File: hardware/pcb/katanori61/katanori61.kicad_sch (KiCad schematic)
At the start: 55 parts, among them J1 XIAO RISER, J10 BAT (JST-PH), J13 USB-C, J2 OLED, J4 SPK IN, J5 SPK OUT, J6 BTN2, J7 REED+TOGGLE, K31 G6S-2F DC5, Q1 MMUN2133LT1G, Q2 AO3401A, Q31 SS8050, U1 TPS61090RSAR, U2 MCP73871-2CCI/ML, U3 INA226AIDGSR, U4 AS5600-ASOM

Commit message: pcb v6.1: AS5600 を ASOT C499458 へ（ASOM C79815 とはリールの大きさだけ違う・📄 データシート 38 ページ。在庫 378 → 6726・単価 $1.76 → $1.36。JLCPCB のプレビューで U4 の向きを確かめた）
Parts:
- U4: value AS5600-ASOM -> AS5600-ASOT; LCSC C79815 -> C499458
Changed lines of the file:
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@@
 			)
 		)
-		(property "Value" "AS5600-ASOM"
+		(property "Value" "AS5600-ASOT"
 			(at 347.98 173.38 0)
 			(effects
@@
 			)
 		)
-		(property "LCSC" "C79815"
+		(property "LCSC" "C499458"
 			(at 347.98 165.10 0)
 			(effects

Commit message: pcb v6.1: MCP73871 をテープ＆リール品 C511310（MCP73871T-2CCI/ML）へ（T は梱包だけ・📄 データシート PRODUCT IDENTIFICATION。$4.41 → $2.19・在庫 2410。5 枚の見積り $110.68 → $99.52。JLCPCB のプレビューで U2 の向きを確かめた）
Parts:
- U2: LCSC C5121473 -> C511310
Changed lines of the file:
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@@
 			)
 		)
-		(property "LCSC" "C5121473"
+		(property "LCSC" "C511310"
 			(at 43.18 154.94 0)
 			(effects

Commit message: pcb v6.1: 表示灯を外す（LED1〜4・R5・R8・R14・R20・Q1 の 9 個）／C7 を U2 の VLIPO の隣へ
- ユーザー「LED は本来不要」。PowerBoost の LED 4 つとそれだけに要る 5 個を回路図と板から消した。
  LBO・STAT1・STAT2 はオープンドレインなので何もつながない。LBI の分圧 R1・R2 は残す
  （📄 TPS61090 9.3.7「LBI を浮かせない」）。check_sch.py の DROPPED に同じ 9 個
- 引き直しで C7（VLIPO）への枝が内層 11.4mm・21mΩ になった（前も裏 7.5mm）。C6・C9 と同じ轍なので
  C7 を U2 の 16 番の右上へ寄せ、c7_link・u2_16_link で先に引く（VLIPO 16.2 → 3.3mm・17 → 5mΩ）。
  C41 は U3 の V33 の真上へ（3.6 → 2.1mm）、R6・R7 は空いた列へ
- DRC エラー 0・未接続 0・すきま不足 0・シルクを絵で確認・筐体の当たり 新しい 0 件（レジン・ナイロン）・
  check_fab 合わない所なし。部品 30 種類 48 個 → 25 種類 39 個（拡張 9 種類）
- ⚠ pad_box() は 90°／270° の部品で幅と高さを入れ替えて返す（c7_link は避けて書いた。関数は未修正）
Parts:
- removed C31: 0.1uF, Capacitor_SMD:C_0805_2012Metric, symbol Device:C_Small
- removed LED1: RED, LED_SMD:LED_0805_2012Metric, symbol Device:LED_Small
- removed LED2: WHITE, LED_SMD:LED_0805_2012Metric, symbol Device:LED_Small
- removed LED3: GREEN, LED_SMD:LED_0805_2012Metric, symbol Device:LED_Small
- removed LED4: YELLOW, LED_SMD:LED_0805_2012Metric, symbol Device:LED_Small
- removed Q1: MMUN2133LT1G, Package_TO_SOT_SMD:SOT-23, symbol Transistor_BJT:Q_PNP_BRT_BEC
- removed R14, R20, R5, R8: 1K, Resistor_SMD:R_0805_2012Metric, symbol Device:R_Small
- removed R44, R45: 5.1k, Resistor_SMD:R_0805_2012Metric, symbol Device:R_Small
- added C41: 0.1uF, Capacitor_SMD:C_0805_2012Metric, symbol Device:C_Small
- added R41: 10m, Resistor_SMD:R_1206_3216Metric, symbol Device:R_Small
- added R42: 10K, Resistor_SMD:R_0805_2012Metric, symbol Device:R_Small
- C31: renamed from Q2; value AO3401A -> 0.1uF; footprint Package_TO_SOT_SMD:SOT-23 -> Capacitor_SMD:C_0805_2012Metric; symbol Transistor_FET:Q_PMOS_GSD -> Device:C_Small; LCSC C15127 -> C49678; Note 逆接保護（P-ch）。1=G・2=S・3=D は AO3401A の SOT-23 の並び。📄 LCSC C15127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 -> relay_board C1
- Q2: renamed from R42; value 10K -> AO3401A; footprint Resistor_SMD:R_0805_2012Metric -> Package_TO_SOT_SMD:SOT-23; symbol Device:R_Small -> Transistor_FET:Q_PMOS_GSD; LCSC C17414 -> C15127; Note I2C の引き上げ -> 逆接保護（P-ch）。1=G・2=S・3=D は AO3401A の SOT-23 の並び。📄 LCSC C15127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
- R44: renamed from R41; value 10m -> 5.1k; footprint Resistor_SMD:R_1206_3216Metric -> Resistor_SMD:R_0805_2012Metric; LCSC C105362 -> C27834; Note シャント 10mΩ（今のモジュールと同じ値）。🔴 ケルビン必須 — gen_pcb.py の PRE_TRACKS を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 -> CC1 の引き下げ（充電器に 5V を出させる）
- R45: renamed from C41; value 0.1uF -> 5.1k; footprint Capacitor_SMD:C_0805_2012Metric -> Resistor_SMD:R_0805_2012Metric; symbol Device:C_Small -> Device:R_Small; LCSC C49678 -> C27834; Note (none) -> CC2 の引き下げ
- U2: Note 充電・ロードシェア（PowerBoost U2） -> 充電・ロードシェア（PowerBoost U2）。MCP73871T-2CCI/ML ── T はテープ＆リールだけ（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
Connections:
- net BATG: now also Q2.1 (G); no longer C31.1 (G)
- net BATP: now also Q2.2 (S), R41.1; no longer C31.2 (S), R44.1
- net BATRAW: now also Q2.3 (D); no longer C31.3 (D)
- net CC1: now also R44.1
- net CC2: now also R45.1
- net GND: now also C31.2, R44.2, C41.2
- net SDA: now also R42.2; no longer Q2.2
- net V33: now also C41.1, R42.1; no longer Q2.1, R45.1
- net V5: now also C31.1
- net VLIPO: now also R41.2; no longer R44.2
- net LBO: no longer names the net of U1.12 (LBO)
- net STAT1: no longer names the net of U2.8 (STAT1/~{LBO})
- net STAT2: no longer names the net of U2.7 (STAT2)
- no-connect marks 15 -> 18
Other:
- moved on the sheet: R44

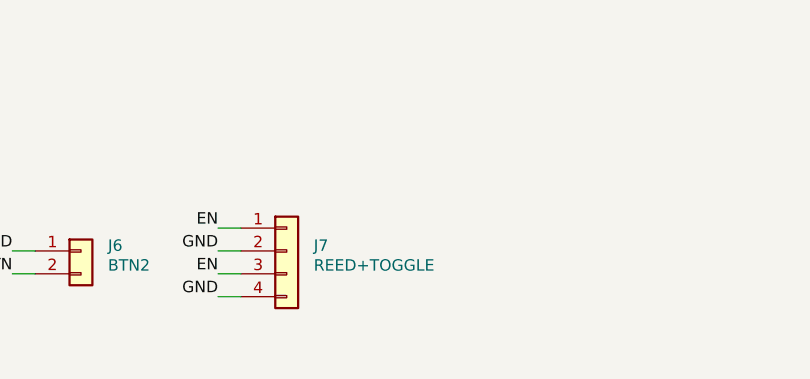
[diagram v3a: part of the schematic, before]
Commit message: v6.1: 電源をハッチのトグルから PCB の押しボタン SW2（XKB5858-Z-E）へ／つまみを左へ 2.0・軸ガイドの穴 3 つ／つまみの台座を直す
電源（🔒 ユーザー 2026-09-19）
- ハッチのトグル MTS-102（座・M6 の穴・線 2 本）をやめ、PCB の後ろの縁、USB-C の左隣に横向き・自己保持の押しボタン SW2（XKB5858-Z-E・LCSC C780038・押し子 5.0）
- 接点 1 GND・3 EN（1–3 は出ている間に閉 ＝ OFF。接点の図とピンの前後の並びの両方から確定）。J7 はリードだけの 2 ピン
- 押し子に丸いキャップ（φ6.6・顔の芯を USB-C の口の芯の高さに揃える・鍔で抜け止め・顔に電源の記号）。キャップは光造形で刷る（print_pwrcap）。断面の模型 part="look_pwrcap"
- 後ろの壁に φ7.1 の丸穴。PCB を入れるときの前逃がし pcb_fwd 1.8 → 3.6（キャップの顔）。C31 は SW2 と重なったので SW2 の前へ固定
- 足形 katanori.pretty/SW_XKB5858-Z-E（パッドは JLC の足形のまま）と記号を追加。parts/mts102_v61.scad を削除

つまみ
- 軸を左へ 2.0（v61_board.SHAFT・KNOB_AT 67.7 → 65.7）。U4・C42・立入禁止・電池の線の道は SHAFT から引く
- 軸ガイドの足の穴 3 つ（M2 φ2.2・半径 12・120° 等分）を取付穴の一覧へ
- 天板の台座: 足 4 本を高さで切り落として段（ナットの六角穴と E リングの受け）ごと消していたのを戻す（knob_station_add(arms=false)）
- リードの穴の入口を掘り上げて押し込む距離 8.0 → 4.5（天井は据え置き）。右後ろの隅を柱の逃げの外まで丸める
- E リングを 1 枚ずつ色分けし、分解図で上下に離す

検査: 回路図 0 件・DRC 未接続 0・製造ファイル「合わない所なし」。当たり・入れる道はナイロン／レジンとも新しい当たり 0（トグルの線と E リングの当たりは線ごと消えた）
格子・支柱・部品表・3D 模型・製造ファイル・発注用 STL を作り直した。組み立てマニュアルは文と番号だけ直した（挿絵と HTML は未）
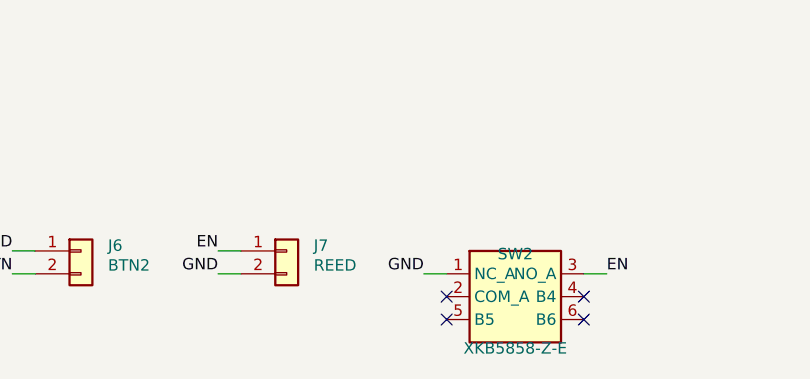
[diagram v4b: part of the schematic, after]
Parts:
- added SW2: XKB5858-Z-E, katanori:SW_XKB5858-Z-E, symbol katanori:SW_XKB5858-Z-E
- J7: value REED+TOGGLE -> REED; footprint Connector_JST:JST_PH_B4B-PH-K_1x04_P2.00mm_Vertical -> Connector_JST:JST_PH_B2B-PH-K_1x02_P2.00mm_Vertical; symbol Connector_Generic:Conn_01x04 -> Connector_Generic:Conn_01x02; Note 1 EN・2 GND → リード ／ 3 EN・4 GND → マスタートグル（縦の口・上から挿す） -> 1 EN・2 GND → リード（縦の口・上から挿す）
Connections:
- net EN: now also SW2.3 (NO_A); no longer J7.3 (Pin_3)
- net GND: now also SW2.1 (NC_A); no longer J7.4 (Pin_4)
- no-connect marks 18 -> 22
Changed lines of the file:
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@@
 	)
 	(symbol
-		(lib_id "Connector_Generic:Conn_01x04")
+		(lib_id "Connector_Generic:Conn_01x02")
 		(at 132.08 243.84 0)
 		(unit 1)
@@
 			)
 		)
-		(property "Value" "REED+TOGGLE"
+		(property "Value" "REED"
 			(at 135.08 245.44 0)
 			(effects
@@
 			)
 		)
-		(property "Footprint" "Connector_JST:JST_PH_B4B-PH-K_1x04_P2.00mm_Vertical"
+		(property "Footprint" "Connector_JST:JST_PH_B2B-PH-K_1x02_P2.00mm_Vertical"
 			(at 132.08 243.84 0)
 			(effects
@@
 			)
 		)
-		(property "Note" "1 EN・2 GND → リード ／ 3 EN・4 GND → マスタートグル（縦の口・上から挿す）"
+		(property "Note" "1 EN・2 GND → リード（縦の口・上から挿す）"
 			(at 132.08 243.84 0)
 			(effects
@@
 		)
 		(pin "2"
-		)
-		(pin "3"
-		)
-		(pin "4"
 		)
 		(instances
@@
 	(wire
 		(pts
-			(xy 127.00 241.30)
-			(xy 124.46 241.30)
-		)
-		(stroke
-			(width 0)
-			(type default)
-		)
-	)
-	(label "EN"
-		(at 124.46 241.30 180)
-		(effects
-			(font
-				(size 1.27 1.27)
-			)
-			(justify right bottom)
-		)
-	)
-	(wire
-		(pts
 			(xy 127.00 243.84)
 			(xy 124.46 243.84)
@@
 		)
 	)
-	(label "GND"
+	(label "EN"
 		(at 124.46 243.84 180)
 		(effects
@@
 		)
 	)
+	(label "GND"
+		(at 124.46 246.38 180)
+		(effects
+			(font
+				(size 1.27 1.27)
+			)
+			(justify right bottom)
+		)
+	)
+	(symbol
+		(lib_id "katanori:SW_XKB5858-Z-E")
+		(at 157.48 248.92 0)
+		(unit 1)
+		(exclude_from_sim no)
+		(in_bom yes)
+		(on_board yes)
+		(dnp no)
+		(property "Reference" "SW2"
+			(at 157.48 244.18 0)
+			(effects
+				(font
+					(size 1.27 1.27)
+				)
+			)
+		)
+		(property "Value" "XKB5858-Z-E"
+			(at 157.48 254.66 0)
+			(effects
+				(font
+					(size 1.27 1.27)
+				)
+			)
+		)
+		(property "Footprint" "katanori:SW_XKB5858-Z-E"
+			(at 157.48 248.92 0)
+			(effects
+				(font
+					(size 1.27 1.27)
+				)
+				(hide yes)
+			)
+		)
+		(property "Datasheet" ""
+			(at 157.48 248.92 0)
+			(effects
+				(font
+					(size 1.27 1.27)
+				)
+				(hide yes)
+			)
+		)
+		(property "LCSC" "C780038"
+			(at 157.48 248.92 0)
+			(effects
+				(font
+					(size 1.27 1.27)
+				)
+				(hide yes)
+			)
+		)
+		(property "Note" "電源の押しボタン（板の後ろの縁・押し子は後ろの壁から出る）。1 GND・3 EN"
+			(at 157.48 248.92 0)
+			(effects
+				(font
+					(size 1.27 1.27)
+				)
+				(hide yes)
+			)
+		)
+		(pin "1"
+		)
+		(pin "2"
+		)
+		(pin "5"
+		)
+		(pin "3"
+		)
+		(pin "4"
+		)
+		(pin "6"
+		)
+		(instances
+			(project "katanori61"
+				(path "/377120ba-3fb3-530c-9f35-c36cf0274025"
+					(reference "SW2")
+					(unit 1)
+				)
+			)
+		)
+	)
+	(wire
+		(pts
+			(xy 149.86 246.38)
+			(xy 147.32 246.38)
+		)
+		(stroke
+			(width 0)
+			(type default)
+		)
+	)
+	(label "GND"
+		(at 147.32 246.38 180)
+		(effects
+			(font
+				(size 1.27 1.27)
+			)
+			(justify right bottom)
+		)
+	)
+	(no_connect
+		(at 149.86 248.92)
+	)
+	(no_connect
+		(at 149.86 251.46)
+	)
+	(wire
+		(pts
+			(xy 165.10 246.38)
+			(xy 167.64 246.38)
+		)
+		(stroke
+			(width 0)
+			(type default)
+		)
+	)
 	(label "EN"
-		(at 124.46 246.38 180)
-		(effects
-			(font
-				(size 1.27 1.27)
-			)
-			(justify right bottom)
-		)
-	)
-	(wire
-		(pts
-			(xy 127.00 248.92)
-			(xy 124.46 248.92)
-		)
-		(stroke
-			(width 0)
-			(type default)
-		)
-	)
-	(label "GND"
-		(at 124.46 248.92 180)
-		(effects
-			(font
-				(size 1.27 1.27)
-			)
-			(justify right bottom)
-		)
+		(at 167.64 246.38 0)
+		(effects
+			(font
+				(size 1.27 1.27)
+			)
+			(justify left bottom)
+		)
+	)
+	(no_connect
+		(at 165.10 248.92)
+	)
+	(no_connect
+		(at 165.10 251.46)
 	)
 	(symbol

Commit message: pcb v6.1: 低電池の分圧を外して LBI を GND へ／詰まっていた 4 組を開ける／角度センサの座標を式に
・R1 1.87M・R2 330K（低電池の分圧）を外し、LBI（U1 の 9 番）を GND へ直結。
  LBO は未接続で閾値 3.33V を誰も読まず、低電池は INA226 が I2C で読むので重複していた。
  📄 TPS61090/91/92 SLVS484C 12 ページ 9.3.7「使わないなら LBI は GND（か VBAT）へ繋げ。
  LBO は繋がなくてよい」── 浮かせなければよいのではなく繋げと書いてあり、分圧である必要は無い。
  機械に載せる部品 39 → 37 個・JLCPCB へ出す品番 26 → 24 種類（330kΩ C23137 は R2 だけが使っていた）。
  ⚠ 2026-09-19 に「分圧は残した」と POWER.md に書かれていたが、それは 🔒 の段落の中に
  AI 側がその場で決めた物を混ぜて書いたもので、ユーザーには聞いていなかった。

・胴どうしが 1mm を切っていた 4 組を開けた。R31–R32 0.75 → 1.55・R44–R45 0.85 → 1.60・
  R42–R43 0.85 → 1.45・R46–J2 0.94 → 1.44mm。R45 は VBUS の幹があるので動かさず、R44 だけ右へ。
  周りで狭くなった所は無い（いちばん近いのは Q2–R31 の 1.02mm で、前の 9 番目 0.98mm より広い）。
  板全体の最小は L1–R3 の 0.67mm のままにした。ここを開けるのは電源の塊をほどく話になる。

・v61_board.py の AS5600 = (65.7, 13.8) を消し、SHAFT から出す式にした。2026-09-19 に
  つまみを左へ 2.0 動かしたときの取り残しで、部品を置くコードは読んでいないので板は正しかったが、
  リレーとの距離の根拠だけ 2mm ずれていた。実測は 18.5mm・磁石の影響は 7.4 分の 1（20mm・9 分の 1 は誤り）。

・裏のシルクの日付を 2026-09-20 へ。

見送り: 音の 3 本（SPKM・SPKO・SPKP）を内層から外層へ手で引き直す案。284 → 150mΩ になるが、
8Ω に対して P ∝ R/(R+r)² なので 0.14dB にしかならず聞こえない。元の 720mΩ でさえ 0.35dB だった。
銅は測り直して 284mΩ（POWER.md の 208mΩ は 9/17 にリレーを角度センサの横から退ける前の値で、
退けたぶん SPKO が 25 → 49mm に伸びていた）。割合ではなく dB で見ること、を POWER.md に残した。

検査: 回路図の突き合わせ 0 件（写し元との意図した差に LBI を登録）・DRC 9 件（前と同じ取付穴の
足形 7・USB-C のシルクが縁で切れる 2）・未配線 0・回路図との食い違い 0・銅のすきま 0 件（最小 0.152）・
製造ファイルの照合 合わない所なし・掃引はナイロンとレジンとも「入る」新しい当たり 0 件。
電源の道は測り直して悪化なし（3.3V は自動配線が裏を使ったぶん 366 → 148mΩ）。
模型（v61_parts.scad・v61_parts3d.stl・v61_silk.scad）も作り直した。板と口の STL は中身が同じ。
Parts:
- removed J10: BAT (JST-PH), Connector_JST:JST_PH_B2B-PH-K_1x02_P2.00mm_Vertical, symbol Connector_Generic:Conn_01x02
- removed J13: USB-C, Connector_USB:USB_C_Receptacle_HRO_TYPE-C-31-M-12, symbol Connector:USB_C_Receptacle_USB2.0_16P
- removed J2: OLED, Connector_PinHeader_2.54mm:PinHeader_1x04_P2.54mm_Vertical, symbol Connector_Generic:Conn_01x04
- removed J5: SPK OUT, Connector_JST:JST_PH_S2B-PH-K_1x02_P2.00mm_Horizontal, symbol Connector_Generic:Conn_01x02
- removed Q2: AO3401A, Package_TO_SOT_SMD:SOT-23, symbol Transistor_FET:Q_PMOS_GSD
- removed Q31: SS8050, Package_TO_SOT_SMD:SOT-23, symbol Transistor_BJT:MMBT3904
- removed R15: 15K, Resistor_SMD:R_0805_2012Metric, symbol Device:R_Small
- removed R32: 10k, Resistor_SMD:R_0805_2012Metric, symbol Device:R_Small
- removed SW2: XKB5858-Z-E, katanori:SW_XKB5858-Z-E, symbol katanori:SW_XKB5858-Z-E
- removed U3: INA226AIDGSR, Package_SO:TSSOP-10_3x3mm_P0.5mm, symbol Sensor_Energy:INA226
- removed U4: AS5600-ASOT, Package_SO:SOIC-8_3.9x4.9mm_P1.27mm, symbol katanori:AS5600-ASOM
- added C31, C41, C42: 0.1uF, Capacitor_SMD:C_0805_2012Metric, symbol Device:C_Small
- added J4: SPK IN, Connector_JST:JST_PH_B2B-PH-K_1x02_P2.00mm_Vertical, symbol Connector_Generic:Conn_01x02
- added J6: BTN2, Connector_JST:JST_PH_B2B-PH-K_1x02_P2.00mm_Vertical, symbol Connector_Generic:Conn_01x02
- added R31: 1k, Resistor_SMD:R_0805_2012Metric, symbol Device:R_Small
- added R41: 10m, Resistor_SMD:R_1206_3216Metric, symbol Device:R_Small
- added R44: 5.1k, Resistor_SMD:R_0805_2012Metric, symbol Device:R_Small
- added R46: 100K, Resistor_SMD:R_0805_2012Metric, symbol Device:R_Small
- C7: renamed from R13; value 200K -> 10uF; footprint Resistor_SMD:R_0805_2012Metric -> Capacitor_SMD:C_0805_2012Metric; symbol Device:R_Small -> Device:C_Small; LCSC C17539 -> C15850
- C8: renamed from R2; value 330K -> 10uF; footprint Resistor_SMD:R_0603_1608Metric -> Capacitor_SMD:C_0805_2012Metric; symbol Device:R_Small -> Device:C_Small; LCSC C23137 -> C15850; Note PowerBoost は 340kΩ（E96・Extended）。LBO の閾値 0.5×(1+R1/R2) が 3.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 -> (none)
- J10: renamed from R42; value 10K -> BAT (JST-PH); footprint Resistor_SMD:R_0805_2012Metric -> Connector_JST:JST_PH_B2B-PH-K_1x02_P2.00mm_Vertical; symbol Device:R_Small -> Connector_Generic:Conn_01x02; LCSC C17414 -> (none); Note I2C の引き上げ -> 🔴 1 番が −・2 番が ＋（PowerBoost B1 の並び。⭐ 2026-09-16 夕から 2 番のネットは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
- J13: renamed from R43; value 10K -> USB-C; footprint Resistor_SMD:R_0805_2012Metric -> Connector_USB:USB_C_Receptacle_HRO_TYPE-C-31-M-12; symbol Device:R_Small -> Connector:USB_C_Receptacle_USB2.0_16P; LCSC C17414 -> C165948; Note I2C の引き上げ -> 充電の口。D+/D− と SBU は使わない。v6.1 は板の後ろの縁から 1.3 出し（⭐ 2026-09-17）で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
- J2: renamed from J4; value SPK IN -> OLED; footprint Connector_JST:JST_PH_B2B-PH-K_1x02_P2.00mm_Vertical -> Connector_PinHeader_2.54mm:PinHeader_1x04_P2.54mm_Vertical; symbol Connector_Generic:Conn_01x02 -> Connector_Generic:Conn_01x04; Note IN（ReSpeakerから） -> AS5600 へ4本（GNDは二股ケーブルでDIRへ）
- J5: renamed from C42; value 0.1uF -> SPK OUT; footprint Capacitor_SMD:C_0805_2012Metric -> Connector_JST:JST_PH_S2B-PH-K_1x02_P2.00mm_Horizontal; symbol Device:C_Small -> Connector_Generic:Conn_01x02; LCSC C49678 -> (none); Note AS5600 のパスコン（📄 9 ページ Figure 13） -> OUT（スピーカーへ）
- Q2: renamed from R44; value 5.1k -> AO3401A; footprint Resistor_SMD:R_0805_2012Metric -> Package_TO_SOT_SMD:SOT-23; symbol Device:R_Small -> Transistor_FET:Q_PMOS_GSD; LCSC C27834 -> C15127; Note CC1 の引き下げ（充電器に 5V を出させる） -> 逆接保護（P-ch）。1=G・2=S・3=D は AO3401A の SOT-23 の並び。📄 LCSC C15127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
- Q31: renamed from R31; value 1k -> SS8050; footprint Resistor_SMD:R_0805_2012Metric -> Package_TO_SOT_SMD:SOT-23; symbol Device:R_Small -> Transistor_BJT:MMBT3904; LCSC C17513 -> C2150; Note relay_board R1 -> relay_board Q1（2SC1815-GR の表面実装の代わり・SOT-23 は 1=B・2=E・3=C）
- R13: renamed from R1; value 1.87M -> 200K; LCSC C482988 -> C17539
- R15: renamed from R16; value 1.0K -> 15K; LCSC C17513 -> C17475; Note (none) -> PowerBoost THERM
- R16: renamed from R6; value 220K -> 1.0K; footprint Resistor_SMD:R_0603_1608Metric -> Resistor_SMD:R_0805_2012Metric; LCSC C22961 -> C17513; Note PowerBoost は 270kΩ（E96・Extended）。R7 と組で比を保つ -> (none)
- R17: renamed from R7; value 82K -> 100K; footprint Resistor_SMD:R_0603_1608Metric -> Resistor_SMD:R_0805_2012Metric; LCSC C23254 -> C149504; Note PowerBoost は 100kΩ。R6 と組で 100/370=0.2703 → 82/302=0.2715（差 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 -> (none)
- R32: renamed from R46; value 100K -> 10k; LCSC C149504 -> C17414; Note Q2 のゲートを GND へ落とす。電池は 3.0〜4.2V なので Vgs は最大 −4.2V で、AO3401A 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 -> relay_board R2・🔴 安全の要
- R42: renamed from R41; value 10m -> 10K; footprint Resistor_SMD:R_1206_3216Metric -> Resistor_SMD:R_0805_2012Metric; LCSC C105362 -> C17414; Note シャント 10mΩ（今のモジュールと同じ値）。🔴 ケルビン必須 — gen_pcb.py の PRE_TRACKS を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 -> I2C の引き上げ
- R43: renamed from C41; value 0.1uF -> 10K; footprint Capacitor_SMD:C_0805_2012Metric -> Resistor_SMD:R_0805_2012Metric; symbol Device:C_Small -> Device:R_Small; LCSC C49678 -> C17414; Note (none) -> I2C の引き上げ
- R6: renamed from C8; value 10uF -> 220K; footprint Capacitor_SMD:C_0805_2012Metric -> Resistor_SMD:R_0603_1608Metric; symbol Device:C_Small -> Device:R_Small; LCSC C15850 -> C22961; Note (none) -> PowerBoost は 270kΩ（E96・Extended）。R7 と組で比を保つ
- R7: renamed from C7; value 10uF -> 82K; footprint Capacitor_SMD:C_0805_2012Metric -> Resistor_SMD:R_0603_1608Metric; symbol Device:C_Small -> Device:R_Small; LCSC C15850 -> C23254; Note (none) -> PowerBoost は 100kΩ。R6 と組で 100/370=0.2703 → 82/302=0.2715（差 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
- SW2: renamed from J6; value BTN2 -> XKB5858-Z-E; footprint Connector_JST:JST_PH_B2B-PH-K_1x02_P2.00mm_Vertical -> katanori:SW_XKB5858-Z-E; symbol Connector_Generic:Conn_01x02 -> katanori:SW_XKB5858-Z-E; LCSC (none) -> C780038; Note 天板の会話ボタンへ 2 本。⭐ 2026-09-16 夕に横出し → **縦**（🔒 ユーザー「J4とJ6を縦にして」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 -> 電源の押しボタン（板の後ろの縁・押し子は後ろの壁から出る）。1 GND・3 EN
- U3: renamed from R17; value 100K -> INA226AIDGSR; footprint Resistor_SMD:R_0805_2012Metric -> Package_SO:TSSOP-10_3x3mm_P0.5mm; symbol Device:R_Small -> Sensor_Energy:INA226; LCSC C149504 -> C49851; Note (none) -> A1=VS・A0=GND → 0x44
- U4: renamed from C31; value 0.1uF -> AS5600-ASOT; footprint Capacitor_SMD:C_0805_2012Metric -> Package_SO:SOIC-8_3.9x4.9mm_P1.27mm; symbol Device:C_Small -> katanori:AS5600-ASOM; LCSC C49678 -> C499458; Note relay_board C1 -> つまみの角度。磁石は真上・板 X 36.2 Y 7。🔴 PGO(5) と OUT(3) は繋がない
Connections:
- net BASE: now also Q31.1 (B), R32.1, R31.2; no longer Q31.2
- net BATG: now also Q2.1 (G), R46.1; no longer R32.1
- net BATP: now also Q2.2 (S), U3.10 (Vin+), R41.1; no longer R42.1
- net BATRAW: now also J10.2 (Pin_2), Q2.3 (D)
- net BTN: now also J6.2 (Pin_2); no longer SW2.2 (Pin_2)
- net CC1: now also J13.A5 (CC1), R44.1; no longer Q2.1
- net CC2: now also J13.B5 (CC2)
- net COL: now also Q31.3 (C)
- net EN: now also R13.2, SW2.3 (NO_A); no longer C7.2
- net GND: now also C7.2, J10.1 (Pin_1), J13.A1 (GND), J13.A12 (GND), J13.B1 (GND), J13.B12 (GND), J13.SH (SHIELD), J2.1 (Pin_1), Q31.2 (E), R16.1, R17.1, U1.9 (LBI), U3.2 (A0), U3.7 (GND), U4.4 (GND), U4.8 (DIR), C31.2, C41.2, C42.2, J6.1 (Pin_1), R44.2, R46.2; no longer J5.2, Q2.2, R17.2, R43.2, R6.2, U3.1, U4.2
- net IN: now also R31.1; no longer Q31.1
- net PROG1: now also R16.2; no longer R15.2
- net PROG3: now also R17.2; no longer U3.2
- net SCL: now also J2.3 (Pin_3), R43.2, U3.5 (SCL), U4.7 (SCL); no longer J13.2
- net SDA: now also J2.4 (Pin_4), R42.2, U3.4 (SDA), U4.6 (SDA); no longer J10.2
- net SPKM: now also J5.1 (Pin_1), J4.2 (Pin_2); no longer J2.2 (Pin_2)
- net SPKO: now also J5.2 (Pin_2)
- net SPKP: now also J4.1 (Pin_1); no longer J2.1 (Pin_1)
- net THERM: now also R15.2
- net V33: now also J2.2 (Pin_2), R42.1, U3.1 (A1), U3.6 (VS), U4.1 (VDD5V), U4.2 (VDD3V3), C41.1, C42.1; no longer J10.1, J13.1, J5.1
- net V5: now also C31.1; no longer U4.1
- net VBUS: now also C8.1, J13.A4 (VBUS), J13.A9 (VBUS), J13.B4 (VBUS), J13.B9 (VBUS); no longer R16.1
- net VLIPO: now also C7.1, U3.8 (Vbus), U3.9 (Vin-), R41.2; no longer R42.2, R7.1
- net VPCC: now also R6.2, R7.1; no longer R16.2, R17.1
- net VSYS: no longer C7.1
- removed net LBI: C8.1, R13.2, U1.9 (LBI)
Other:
- moved on the sheet: R15, R16, R17, R32, R42
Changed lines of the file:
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@@
 		)
 	)
-	(label "LBI"
+	(label "GND"
 		(at 22.86 48.26 180)
 		(effects
@@
 		(on_board yes)
 		(dnp no)
-		(property "Reference" "R1"
+		(property "Reference" "R13"
 			(at 149.12 40.04 0)
 			(effects
@@
 			)
 		)
-		(property "Value" "1.87M"
+		(property "Value" "200K"
 			(at 149.12 42.24 0)
 			(effects
@@
 			)
 		)
-		(property "LCSC" "C482988"
+		(property "LCSC" "C17539"
 			(at 147.32 40.64 0)
-			(effects
-				(font
-					(size 1.27 1.27)
-				)
-				(hide yes)
-			)
-		)
-		(pin "1"
-		)
-		(pin "2"
-		)
-		(instances
-			(project "katanori61"
-				(path "/377120ba-3fb3-530c-9f35-c36cf0274025"
-					(reference "R1")
-					(unit 1)
-				)
-			)
-		)
-	)
-	(wire
-		(pts
-			(xy 147.32 38.10)
-			(xy 147.32 35.56)
-		)
-		(stroke
-			(width 0)
-			(type default)
-		)
-	)
-	(label "VSYS"
-		(at 147.32 35.56 90)
-		(effects
-			(font
-				(size 1.27 1.27)
-			)
-			(justify left bottom)
-		)
-	)
-	(wire
-		(pts
-			(xy 147.32 43.18)
-			(xy 147.32 45.72)
-		)
-		(stroke
-			(width 0)
-			(type default)
-		)
-	)
-	(label "LBI"
-		(at 147.32 45.72 270)
-		(effects
-			(font
-				(size 1.27 1.27)
-			)
-			(justify right bottom)
-		)
-	)
-	(symbol
-		(lib_id "Device:R_Small")
-		(at 160.02 40.64 0)
-		(unit 1)
-		(exclude_from_sim no)
-		(in_bom yes)
-		(on_board yes)
-		(dnp no)
-		(property "Reference" "R2"
-			(at 161.82 40.04 0)
-			(effects
-				(font
-					(size 1.27 1.27)
-				)
-				(justify left)
-			)
-		)
-		(property "Value" "330K"
-			(at 161.82 42.24 0)
-			(effects
-				(font
-					(size 1.27 1.27)
-				)
-				(justify left)
-			)
-		)
-		(property "Footprint" "Resistor_SMD:R_0603_1608Metric"
-			(at 160.02 40.64 0)
-			(effects
-				(font
-					(size 1.27 1.27)
-				)
-				(hide yes)
-			)
-		)
-		(property "Datasheet" ""
-			(at 160.02 40.64 0)
-			(effects
-				(font
-					(size 1.27 1.27)
-				)
-				(hide yes)
-			)
-		)
-		(property "LCSC" "C23137"
-			(at 160.02 40.64 0)
-			(effects
-				(font
-					(size 1.27 1.27)
-				)
-				(hide yes)
-			)
-		)
-		(property "Note" "PowerBoost は 340kΩ（E96・Extended）。LBO の閾値 0.5×(1+R1/R2) が 3.25V → 3.33V"
-			(at 160.02 40.64 0)
-			(effects
-				(font
-					(size 1.27 1.27)
-				)
-				(hide yes)
-			)
-		)
-		(pin "1"
-		)
-		(pin "2"
-		)
-		(instances
-			(project "katanori61"
-				(path "/377120ba-3fb3-530c-9f35-c36cf0274025"
-					(reference "R2")
-					(unit 1)
-				)
-			)
-		)
-	)
-	(wire
-		(pts
-			(xy 160.02 38.10)
-			(xy 160.02 35.56)
-		)
-		(stroke
-			(width 0)
-			(type default)
-		)
-	)
-	(label "LBI"
-		(at 160.02 35.56 90)
-		(effects
-			(font
-				(size 1.27 1.27)
-			)
-			(justify left bottom)
-		)
-	)
-	(wire
-		(pts
-			(xy 160.02 43.18)
-			(xy 160.02 45.72)
-		)
-		(stroke
-			(width 0)
-			(type default)
-		)
-	)
-	(label "GND"
-		(at 160.02 45.72 270)
-		(effects
-			(font
-				(size 1.27 1.27)
-			)
-			(justify right bottom)
-		)
-	)
-	(symbol
-		(lib_id "Device:R_Small")
-		(at 170.18 40.64 0)
-		(unit 1)
-		(exclude_from_sim no)
-		(in_bom yes)
-		(on_board yes)
-		(dnp no)
-		(property "Reference" "R13"
-			(at 171.98 40.04 0)
-			(effects
-				(font
-					(size 1.27 1.27)
-				)
-				(justify left)
-			)
-		)
-		(property "Value" "200K"
-			(at 171.98 42.24 0)
-			(effects
-				(font
-					(size 1.27 1.27)
-				)
-				(justify left)
-			)
-		)
-		(property "Footprint" "Resistor_SMD:R_0805_2012Metric"
-			(at 170.18 40.64 0)
-			(effects
-				(font
-					(size 1.27 1.27)
-				)
-				(hide yes)
-			)
-		)
-		(property "Datasheet" ""
-			(at 170.18 40.64 0)
-			(effects
-				(font
-					(size 1.27 1.27)
-				)
-				(hide yes)
-			)
-		)
-		(property "LCSC" "C17539"
-			(at 170.18 40.64 0)
 			(effects
 				(font
@@
 	(wire
 		(pts
-			(xy 170.18 38.10)
-			(xy 170.18 35.56)
+			(xy 147.32 38.10)
+			(xy 147.32 35.56)
 		)
 		(stroke
@@
 	)
 	(label "VSYS"
-		(at 170.18 35.56 90)
-		(effects
-			(font
-				(size 1.27 1.27)
-			)
-			(justify left bottom)
-		)
-	)
-	(wire
-		(pts
-			(xy 170.18 43.18)
-			(xy 170.18 45.72)
+		(at 147.32 35.56 90)
+		(effects
+			(font
+				(size 1.27 1.27)
+			)
+			(justify left bottom)
+		)
+	)
+	(wire
+		(pts
+			(xy 147.32 43.18)
+			(xy 147.32 45.72)
 		)
 		(stroke
@@
 	)
 	(label "EN"
-		(at 170.18 45.72 270)
-		(effects
-			(font
+		(at 147.32 45.72 270)
+		(effects
+			(font
